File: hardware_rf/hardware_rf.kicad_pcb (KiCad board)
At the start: 4 copper layers, 72 x 72 mm, 91 parts, among them IC1 CC1125RHBR, IC2 BALF-SPI2-02D3, IC3 4259-63, IC4 4259-63, J1 Conn_Coaxial, J3 Conn_02x20_Top_Bottom, J4 USB_C_Receptacle_USB2.0_16P, SW1 SW_Push, U1 RP2350A-QFN60, U2 W25Q128JVS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

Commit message: pcb
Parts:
- removed the G*** at (0.00, 0.00)

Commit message: CC lines on USB fixed
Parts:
- added R13: 5.1k, Resistor_SMD:R_0402_1005Metric, F.Cu at (149.1, 131.2)
- added R14: 5.1k, Resistor_SMD:R_0402_1005Metric, F.Cu at (143.2, 132.6)
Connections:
- J4 pad A5: unconnected-(J4-CC1-PadA5) -> Net-(J4-CC1)
- J4 pad B5: unconnected-(J4-CC2-PadB5) -> Net-(J4-CC2)
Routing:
- net Net-(J4-CC2): track 0.00 -> 5.29 mm
- net Net-(J4-CC1): track 0.00 -> 3.50 mm

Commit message: PCB Done
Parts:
- added G***: LOGO, LOGO, F.Cu at (190.0, 107.4)
- added G***: LOGO, LOGO, F.Cu at (146.0, 87.8)
- added G***: LOGO, LOGO, B.Cu at (156.4, 143.6)
- added G***: LOGO, LOGO, B.Cu at (189.7, 108.7)
- added REF**: LayerMarker_4_6.35x2.54mm_TextH1mm_P1.27mm, Symbol:LayerMarker_4_6.35x2.54mm_TextH1mm_P1.27mm, F.Cu at (178.5, 146.2)
- added REF**: ESD-Logo_13.2x12mm_SilkScreen, Symbol:ESD-Logo_13.2x12mm_SilkScreen, B.Cu at (171.9, 133.5)
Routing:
- net GND: track 54.3 -> 96.8 mm, vias 58 -> 90
- net 3v3: track 104.3 -> 109.0 mm, vias 19 -> 21
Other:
- board text added: "ASTRALIS current members Keyaan Khatri - Lead and Communications Jaydev Parmar - Flight Avionics and OBC Dhruvansh Mankad - ADCS and control algorithms Rishaan Sharma - Energy and EPS Dhairya Upadhyay - CAD and Mechanical Design"
- board text added: "I completed this pcb in 4 hours"
- board text added: "Made On Earth By Humans"
- board text removed: "I completed the pcb in 4 hours"
- board text removed: "Made By Humans On Earth"

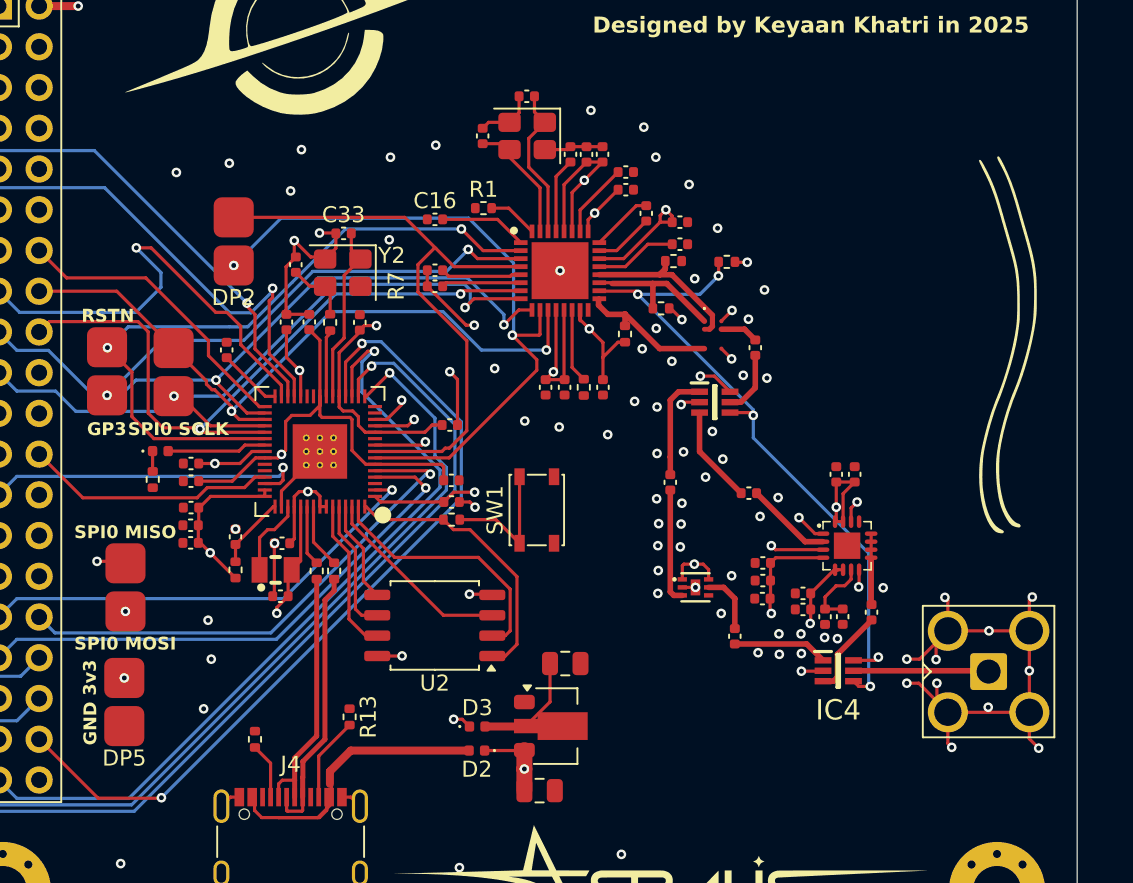
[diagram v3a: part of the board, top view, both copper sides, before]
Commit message: Added SWD to PCB
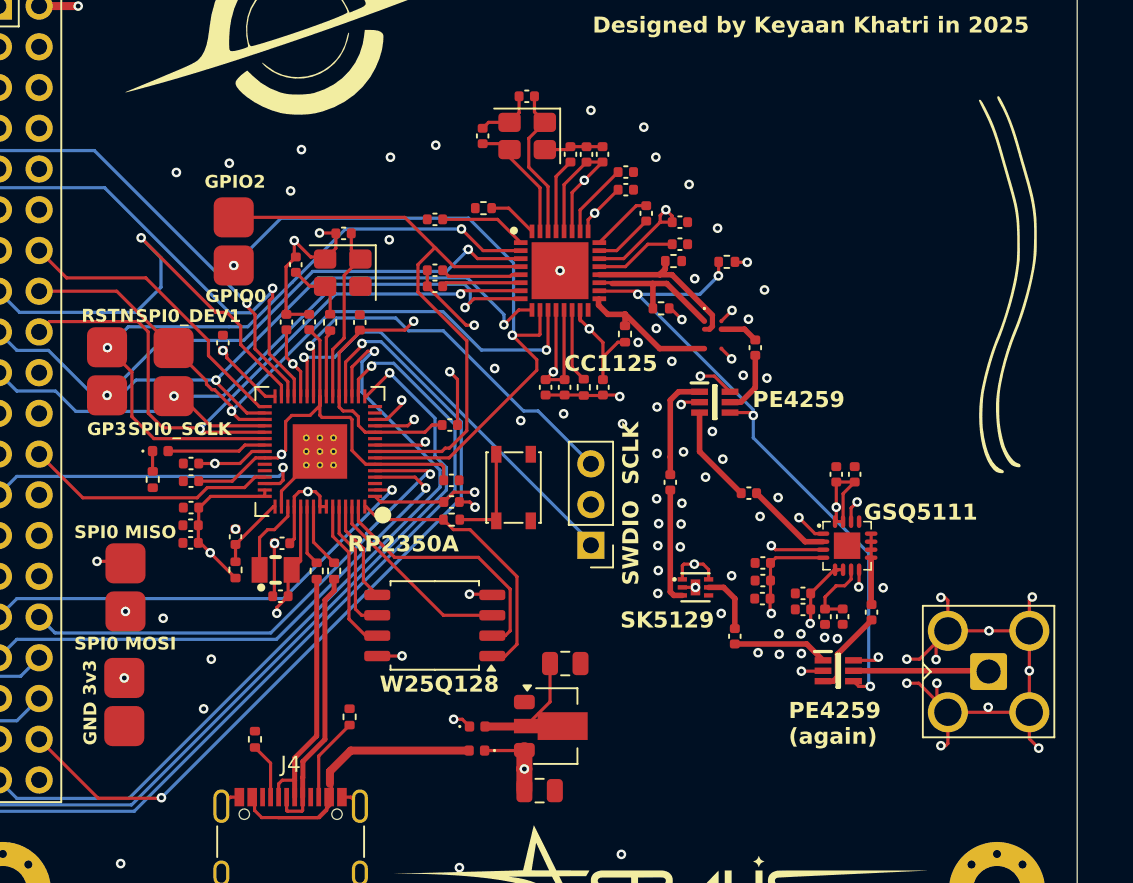
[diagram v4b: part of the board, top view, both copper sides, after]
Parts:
- added J2: Conn_01x03_Socket, Connector_PinHeader_2.54mm:PinHeader_1x03_P2.54mm_Vertical, F.Cu at (164.2, 120.5)
- moved G*** 3.75 mm to (190.0, 103.6)
- moved G*** 3.75 mm to (189.7, 104.9)
- moved SW1 2.02 mm to (159.3, 116.9)
- moved C26 0.50 mm to (141.2, 107.9)
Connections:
- U1 pad 24: unconnected-(U1-SWCLK-Pad24) -> Net-(J2-Pin_3)
- U1 pad 25: unconnected-(U1-SWDIO-Pad25) -> Net-(J2-Pin_1)
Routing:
- net Net-(J2-Pin_1): track 0.00 -> 26.7 mm, vias 0 -> 1
- net Net-(J2-Pin_3): track 0.00 -> 25.3 mm, vias 0 -> 1
- net GND: track 96.8 -> 101.9 mm
- net 3v3: track 109.0 -> 112.0 mm, vias 21 -> 22
- net Net-(R6-Pad1): track 8.49 -> 6.40 mm
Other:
- board text added: "CC1125"
- board text added: "GPIO0"
- board text added: "GPIO2"
- board text added: "GSQ5111"
- board text added: "PE4259"
- board text added: "PE4259 (again)"
- board text added: "RP2350A"
- board text added: "SK5129"
- board text added: "SPI0_DEV1"
- board text added: "SPI0_SCLK"
- board text added: "SWDIO SCLK"
- board text added: "W25Q128"
- board text removed: "SPI0 SCLK"

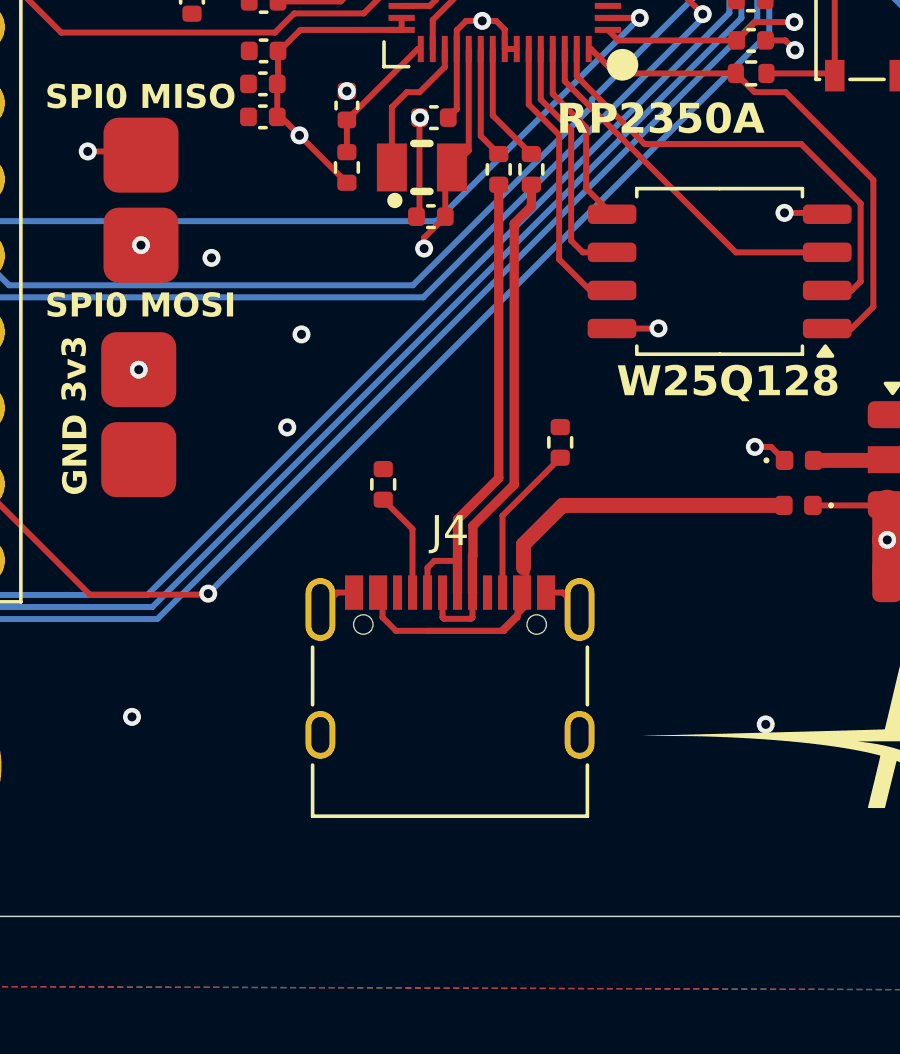
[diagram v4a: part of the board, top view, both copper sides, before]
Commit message: Update USB C Position
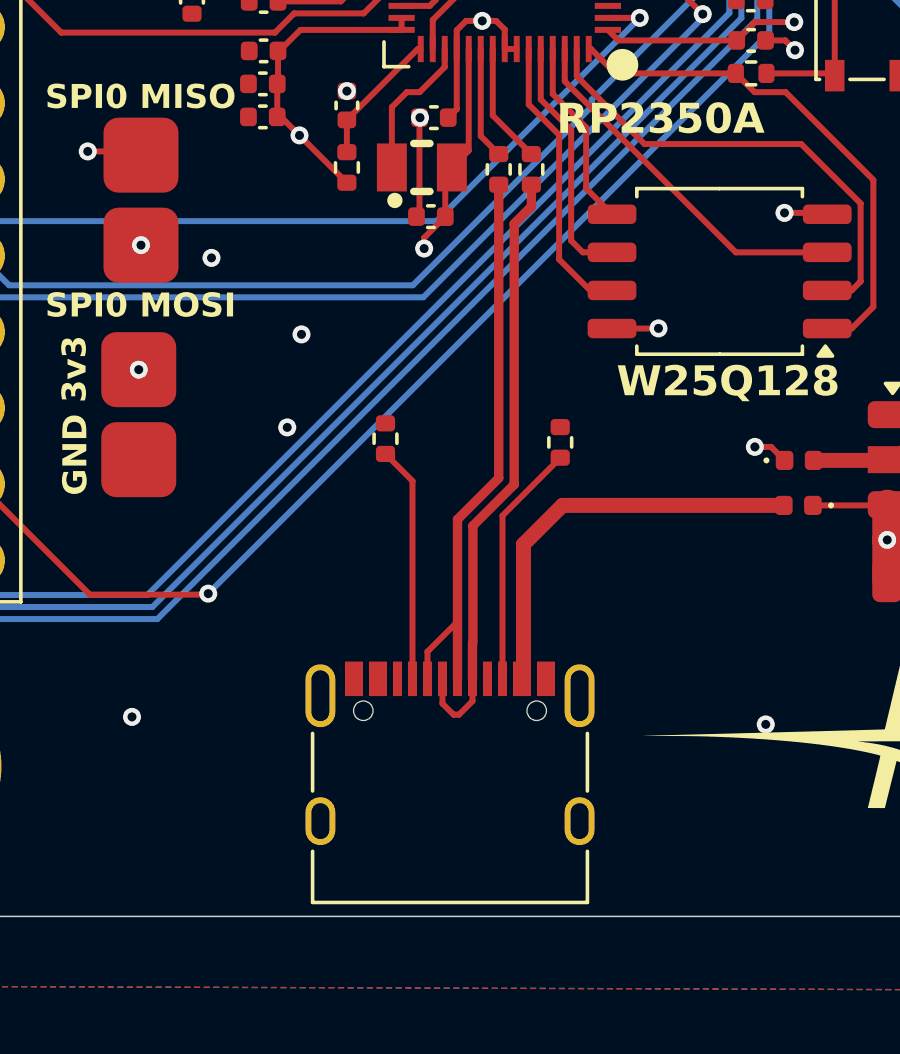
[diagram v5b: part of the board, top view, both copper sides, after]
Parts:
- moved J4 2.88 mm to (145.4, 142.8)
- moved R14 1.53 mm to (143.3, 131.1)
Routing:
- net Net-(D2-A): track 21.6 -> 13.6 mm
- net Net-(J4-CC1): track 3.50 -> 7.87 mm
- net USB_DM: track 16.1 -> 19.4 mm
- net USB_DP: track 17.1 -> 20.2 mm
- net Net-(J4-CC2): track 5.29 -> 8.17 mm
- net GND: track 101.9 -> 99.5 mm
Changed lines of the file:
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@@
 	(footprint "Resistor_SMD:R_0402_1005Metric"
 		(layer "F.Cu")
-		(at 143.225 132.6 -90)
+		(at 143.3 131.075 -90)
 		(descr "Resistor SMD 0402 (1005 Metric), square (rectangular) end terminal, IPC-7351 nominal, (Body size source: IPC-SM-782 page 72, https://www.pcb-3d.com/wordpress/wp-content/uploads/ipc-sm-782a_amendment_1_and_2.pdf), generated with kicad-footprint-generator")
 		(tags "resistor")
@@
 	(footprint "Connector_USB:USB_C_Receptacle_XKB_U262-16XN-4BVC11"
 		(layer "F.Cu")
-		(at 145.45 139.875)
+		(at 145.45 142.75)
 		(descr "USB Type C, right-angle, SMT, https://datasheet.lcsc.com/szlcsc/1811141824_XKB-Enterprise-U262-161N-4BVC11_C319148.pdf")
 		(tags "USB C Type-C Receptacle SMD")
@@
 			(at 0 -5.715 0)
 			(layer "F.SilkS")
+			(hide yes)
 			(effects
 				(font
@@
 	)
 	(segment
-		(start 142.1 136.205)
-		(end 141.695 136.205)
-		(width 0.2)
-		(layer "F.Cu")
-		(net 1)
-	)
-	(segment
-		(start 149.205 136.205)
-		(end 149.77 136.77)
-		(width 0.2)
-		(layer "F.Cu")
-		(net 1)
-	)
-	(segment
 		(start 163.73 111.16)
 		(end 164.895 111.16)
@@
 	)
 	(segment
-		(start 141.695 136.205)
-		(end 141.13 136.77)
-		(width 0.2)
-		(layer "F.Cu")
-		(net 1)
-	)
-	(segment
 		(start 144.4325 120.375)
 		(end 144.4325 123.575)
@@
 	)
 	(segment
-		(start 148.8 136.205)
-		(end 149.205 136.205)
-		(width 0.2)
-		(layer "F.Cu")
-		(net 1)
-	)
-	(segment
 		(start 186.25 123.75)
 		(end 186.435 123.935)
@@
 	)
 	(segment
-		(start 144.7 137.482)
-		(end 147.25 137.482)
-		(width 0.2)
-		(layer "F.Cu")
-		(net 32)
-	)
-	(segment
-		(start 147.7 137.032)
-		(end 147.7 136.205)
-		(width 0.2)
-		(layer "F.Cu")
-		(net 32)
-	)
-	(segment
-		(start 143.2 136.205)
-		(end 143.2 137.032)
-		(width 0.2)
-		(layer "F.Cu")
-		(net 32)
-	)
-	(segment
-		(start 148 136.205)
-		(end 148 135.378)
-		(width 0.2)
-		(layer "F.Cu")
-		(net 32)
-	)
-	(segment
-		(start 147.899 134.601)
-		(end 147.899 135.378)
-		(width 0.5)
-		(layer "F.Cu")
-		(net 32)
-	)
-	(segment
-		(start 147.148 137.482)
-		(end 144.7 137.482)
-		(width 0.2)
-		(layer "F.Cu")
-		(net 32)
-	)
-	(segment
-		(start 143.2 137.032)
-		(end 143.65 137.482)
-		(width 0.2)
-		(layer "F.Cu")
-		(net 32)
-	)
-	(segment
-		(start 143.65 137.482)
-		(end 144.7 137.482)
-		(width 0.2)
-		(layer "F.Cu")
-		(net 32)
-	)
-	(segment
 		(start 156.5775 133.3)
 		(end 149.2 133.3)
@@
 	)
 	(segment
-		(start 148 136.63)
-		(end 147.148 137.482)
-		(width 0.2)
-		(layer "F.Cu")
-		(net 32)
-	)
-	(segment
-		(start 148 136.205)
-		(end 148 136.63)
-		(width 0.2)
-		(layer "F.Cu")
-		(net 32)
-	)
-	(segment
-		(start 147.25 137.482)
-		(end 147.7 137.032)
-		(width 0.2)
+		(start 147.899 134.601)
+		(end 147.899 138.881)
+		(width 0.5)
 		(layer "F.Cu")
 		(net 32)
 	)
 	(segment
-		(start 143.025 136.08)
-		(end 142.9 136.205)
-		(width 0.2)
+		(start 149.2 133.3)
+		(end 147.899 134.601)
+		(width 0.5)
 		(layer "F.Cu")
 		(net 32)
 	)
 	(segment
-		(start 149.2 133.3)
-		(end 147.899 134.601)
+		(start 147.899 138.881)
+		(end 147.801 138.979)
 		(width 0.5)
 		(layer "F.Cu")
@@
 	)
 	(segment
-		(start 144.928 135.15)
-		(end 145.7 135.15)
-		(width 0.2)
+		(start 145.7 133.767215)
+		(end 147.075 132.392215)
+		(width 0.3134)
 		(layer "F.Cu")
 		(net 79)
 	)
 	(segment
-		(start 145.7 135.15)
-		(end 145.7 136.205)
-		(width 0.3134)
+		(start 144.7 138.175)
+		(end 145.7 137.175)
+		(width 0.2)
 		(layer "F.Cu")
 		(net 79)
 	)
 	(segment
-		(start 145.7 133.767215)
-		(end 145.7 135.15)
+		(start 145.7 139.08)
+		(end 145.7 137.175)
 		(width 0.3134)
 		(layer "F.Cu")
@@
 	)
 	(segment
-		(start 144.7 136.205)
-		(end 144.7 135.378)
-		(width 0.2)
+		(start 145.7 137.175)
+		(end 145.7 133.767215)
+		(width 0.3134)
 		(layer "F.Cu")
 		(net 79)
 	)
 	(segment
-		(start 144.7 135.378)
-		(end 144.928 135.15)
+		(start 144.7 139.08)
+		(end 144.7 138.175)
 		(width 0.2)
 		(layer "F.Cu")
@@
 	)
 	(segment
-		(start 147.075 122.61)
-		(end 147.075 132.392215)
-		(width 0.3134)
-		(layer "F.Cu")
-		(net 79)
-	)
-	(segment
 		(start 147.075 132.392215)
-		(end 145.7 133.767215)
+		(end 147.075 122.61)
 		(width 0.3134)
 		(layer "F.Cu")
@@
 	)
 	(segment
-		(start 144.2 134.085)
-		(end 144.2 136.205)
+		(start 144.2 139.08)
+		(end 144.2 132.485)
 		(width 0.2)
 		(layer "F.Cu")
@@
 	)
 	(segment
-		(start 143.225 133.11)
-		(end 144.2 134.085)
+		(start 144.2 132.485)
+		(end 143.3 131.585)
 		(width 0.2)
 		(layer "F.Cu")
@@
 	)
 	(segment
-		(start 149.125 131.716973)
-		(end 149.125 131.71)
+		(start 147.2 133.641973)
+		(end 147.2 139.08)
 		(width 0.2)
 		(layer "F.Cu")
@@
 	)
 	(segment
-		(start 147.2 136.205)
+		(start 149.125 131.716973)
 		(end 147.2 133.641973)
 		(width 0.2)
@@
 	)
 	(segment
-		(start 147.2 133.641973)
+		(start 149.125 131.71)
 		(end 149.125 131.716973)
 		(width 0.2)
@@
 	)
 	(segment
-		(start 147.5894 132.605287)
-		(end 146.2144 133.980287)
+		(start 146.2 139.08)
+		(end 146.2 137.9)
 		(width 0.3134)
 		(layer "F.Cu")
@@
 	)
 	(segment
-		(start 146.2 137.032)
-		(end 146.2 136.205)
-		(width 0.2)
+		(start 148.1625 123.3375)
+		(end 147.5894 123.9106)
+		(width 0.3134)
 		(layer "F.Cu")
 		(net 83)
 	)
 	(segment
-		(start 148.1625 123.3375)
-		(end 147.5894 123.9106)
-		(width 0.3134)
+		(start 145.2 139.907)
+		(end 145.568 140.275)
+		(width 0.2)
 		(layer "F.Cu")
 		(net 83)
 	)
 	(segment
-		(start 147.5894 123.9106)
-		(end 147.5894 132.605287)
-		(width 0.3134)
+		(start 145.75 140.275)
+		(end 146.2 139.825)
+		(width 0.2)
 		(layer "F.Cu")
 		(net 83)
 	)
 	(segment
-		(start 146.2 136.205)
-		(end 146.2 134.975)
-		(width 0.3134)
+		(start 146.2 139.825)
+		(end 146.2 139.08)
+		(width 0.2)
 		(layer "F.Cu")
 		(net 83)
 	)
 	(segment
-		(start 148.1625 122.61)
-		(end 148.1625 123.3375)
+		(start 146.2144 133.980287)
+		(end 146.2144 137.8856)
 		(width 0.3134)
 		(layer "F.Cu")
@@
 	)
 	(segment
-		(start 145.2 136.205)
-		(end 145.2 137.032)
+		(start 146.2 137.9)
+		(end 146.2144 137.8856)
 		(width 0.2)
 		(layer "F.Cu")
@@
 	)
 	(segment
-		(start 145.249 137.081)
-		(end 146.151 137.081)
+		(start 145.2 139.08)
+		(end 145.2 139.907)
 		(width 0.2)
 		(layer "F.Cu")
@@
 	)
 	(segment
-		(start 146.151 137.081)
-		(end 146.2 137.032)
+		(start 147.5894 123.9106)
+		(end 147.5894 132.605287)
+		(width 0.3134)
+		(layer "F.Cu")
+		(net 83)
+	)
+	(segment
+		(start 145.568 140.275)
+		(end 145.75 140.275)
 		(width 0.2)
 		(layer "F.Cu")
@@
 	)
 	(segment
-		(start 146.2144 133.980287)
-		(end 146.2144 134.975)
+		(start 148.1625 122.61)
+		(end 148.1625 123.3375)
 		(width 0.3134)
 		(layer "F.Cu")
@@
 	)
 	(segment
-		(start 145.2 137.032)
-		(end 145.249 137.081)
-		(width 0.2)
+		(start 147.5894 132.605287)
+		(end 146.2144 133.980287)
+		(width 0.3134)
 		(layer "F.Cu")
 		(net 83)

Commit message: added ESD Protection and Moved USB-C Connector pos
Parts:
- added D4: ESDS314DBVR, user_imported_devices:ESDS314BVR_SOT95P280X145-5N, F.Cu at (155.2, 137.5)
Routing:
- net USB_DM: track 19.4 -> 29.9 mm, vias 0 -> 2
- net USB_DP: track 20.2 -> 29.3 mm, vias 0 -> 2
- net Net-(D2-A): track 13.6 -> 22.1 mm, vias 0 -> 2

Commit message: Update PA
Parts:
- U3: value GSQ5111 -> GSQ5110; footprint easyeda2kicad:QFN-16_L3.0-W3.0-P0.50-TL-EP1.65 -> easyeda2kicad:QFN-16_L3.0-W3.0-P0.50-TL-EP2.0
- moved C38 8.43 mm to (177.1, 116.1), turned to -90 degrees
- moved C37 7.46 mm to (178.1, 116.1), turned to -90 degrees
- moved U3 0.99 mm to (179.2, 120.7)
- moved C49 0.50 mm to (181.3, 125.0)
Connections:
- C46 pad 2: Net-(U3-RF_IN) -> Net-(U3-RFIN)
- U3 pad 1: GND -> unconnected-(U3-NC-Pad1)
- U3 pad 13: unconnected-(U3-NC-Pad13) -> GND
- U3 pad 14: GND -> 5v
- U3 pad 15: 5v -> 3v3
- U3 pad 16: 5v -> 3v3
- U3 pad 2: Net-(U3-RF_IN) -> GND
- U3 pad 3: GND -> Net-(U3-RFIN)
- U3 pad 4: 5v -> GND
- U3 pad 5: 3v3 -> 5v
- U3 pad 6: 3v3 -> 5v
- U3 pad 7: Net-(U3-2f0) -> GND
- U3 pad 8: GND -> Net-(U3-2f0)
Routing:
- net 3v3: track 112.0 -> 124.4 mm, vias 22 -> 28
- net GND: track 99.5 -> 111.5 mm, vias 90 -> 124
- net Net-(U3-RF_IN): track 5.40 -> 0.00 mm
- net Net-(U3-RFIN): track 0.00 -> 5.23 mm
- net Net-(U3-2f0): track 4.55 -> 3.19 mm
- added copper zone on F.Cu, net 3v3
